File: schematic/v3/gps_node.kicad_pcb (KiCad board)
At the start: 2 copper layers, 48 x 75 mm, 69 parts, among them IC1 MCP73831/2, J1 Mounting Hole, J11 AVR ICSP, J12 UART RF, J13 LIPO_BAT, J14 SOLAR, J15 UART GPS, J16 FW_UPDATE, J17 u.FL connector, J2 Mounting Hole, J3 Mounting Hole, J4 Mounting Hole, J5 TEST Vbatt, J6 USB_OTG, J7 Test 3.3v, J8 Test Gnd, J9 Test V_bak, SW1 RS stock no. 448-0747, SW2 RESET, SW3 MODE, U1 TLV71333PDBV, U2 ublox-cam-m8q-0, U3 TLV71333PDBV, U4 ATMEGA32U4-AU, U5 RN2483, Y1 16MHz

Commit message: Started PCB layout
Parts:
- removed D2: BAS K73, Diodes_SMD:D_SOT-23_ANK
- removed J14: SOLAR, Connectors_Molex:Molex_PicoBlade_53047-0210_02x1.25mm_Straight
- added C22: 100nF, Capacitors_SMD:C_0805, F.Cu at (96.3, 65.0)
- added C23: 100nF, Capacitors_SMD:C_0805, F.Cu at (86.2, 65.0)
- added C24: 100nF, Capacitors_SMD:C_0805, F.Cu at (86.2, 66.9)
- added C25: 100nF, Capacitors_SMD:C_0805, F.Cu at (89.8, 65.0)
- C2: footprint Capacitors_SMD:C_1206 -> Capacitors_SMD:C_0805
- C3, C5, C6: value 4.7uF -> 10uF
- D3, D4: value LED_Small_ALT -> LED; footprint LEDs:LED_0805 -> LEDs:LED_0805_HandSoldering; moved to B.Cu
- D5: footprint LEDs:LED_0805 -> LEDs:LED_0805_HandSoldering
- D6: footprint LEDs:LED_0805 -> LEDs:LED_0805_HandSoldering; moved to B.Cu
- R12, R13: value 470 -> 1k
- SW2: value RESET -> SW_Push
- SW3: value MODE -> SW_Push
- moved C19 56.9 mm to (80.3, 127.8)
- moved C12 54.7 mm to (82.3, 123.2)
- moved U5 49.5 mm to (66.3, 91.2)
- moved C5 40.5 mm to (71.9, 122.9)
- moved R17 27.1 mm to (83.1, 133.1)
- moved D5 26.8 mm to (83.1, 129.0)
- moved R18 26.8 mm to (85.1, 133.1)
- moved R13 26.3 mm to (87.4, 133.0), turned to 90 degrees
- moved R12 25.9 mm to (89.7, 133.1), turned to 90 degrees
- moved D6 9.63 mm to (115.6, 125.8), turned to 0 degrees
- moved D4 5.24 mm to (115.7, 115.6), turned to 180 degrees
- moved D3 3.55 mm to (115.7, 120.7), turned to 180 degrees
- moved R10 0.19 mm to (105.2, 111.8), turned to 90 degrees
- turned R2 to 270 degrees
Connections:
- net +3V3 renamed V_3.3
- net +BATT renamed V_BATT
- net /MISO renamed /Microcontroller/MISO
- net /MOSI renamed /Microcontroller/MOSI
- net /REG_ENABLE renamed /power/REG_ENABLE
- net /SCK renamed /Microcontroller/SCK
- net /UART_AT_TO_RN renamed /Microcontroller/UART_RN_IN
- net /UART_GPS_OUT renamed /Microcontroller/UART_GPS_OUT
- net /UART_RN_TO_AT renamed /Microcontroller/UART_RN_OUT
- net /V_Charger renamed /power/V_Charger
- net /V_bak renamed V_BAK
- net /charge_status renamed /Microcontroller/CHARGE_STATUS
- net Net-(C1-Pad3) renamed /Sheet5C378858/GPS_POWER
- net Net-(J16-Pad4) renamed /Sheet5C378858/RN_PGD
- net Net-(J16-Pad5) renamed /Sheet5C378858/RN_PGC
- C12 pad 1: /V_RN -> /Sheet5C378858/RN_POWER
- C14 pad 1: Net-(C14-Pad1) -> GND
- C14 pad 2: GND -> Net-(C14-Pad2)
- C15 pad 1: Net-(C15-Pad1) -> GND
- C15 pad 2: GND -> Net-(C15-Pad2)
- C16 pad 1: Net-(C16-Pad1) -> GND
- C16 pad 2: GND -> Net-(C16-Pad2)
- C17 pad 1: Net-(C17-Pad1) -> GND
- C17 pad 2: GND -> Net-(C17-Pad2)
- C19 pad 3: /V_RN -> /Sheet5C378858/RN_POWER
- C20 pad 1: /BAT_MEASURE -> GND
- C20 pad 2: GND -> /Microcontroller/BAT_MEASURE
- C5 pad 1: /V_RN -> /Sheet5C378858/RN_POWER
- D1 pad 2: /V_Solar -> V_BUS
- F1 pad 1: VBUS -> V_BUS
- J11 pad 5: /RESET -> /Microcontroller/RESET
- J15 pad 2: /UART_GPS_IN -> /Microcontroller/UART_GPS_IN
- J16 pad 1: /RN_RESET -> /Microcontroller/RN_RESET
- J16 pad 2: /V_RN -> /Sheet5C378858/RN_POWER
- R10 pad 1: /RN_RESET -> /Sheet5C378858/RN_POWER
- R10 pad 2: /V_RN -> /Microcontroller/RN_RESET
- R11 pad 2: /BUTTON_1 -> /Microcontroller/BUTTON_1
- R12 pad 1: Net-(D3-Pad2) -> /Microcontroller/LED0
- R12 pad 2: /LED_OUT_RED -> Net-(D3-Pad2)
- R13 pad 1: Net-(D4-Pad2) -> /Microcontroller/LED1
- R13 pad 2: /LED_OUT_GRN -> Net-(D4-Pad2)
- R15 pad 2: /BAT_MEASURE -> /Microcontroller/BAT_MEASURE
- R16 pad 1: /BAT_MEASURE -> /Microcontroller/BAT_MEASURE
- R2 pad 1: /UART_GPS_IN -> Net-(R2-Pad1)
- R2 pad 2: Net-(R2-Pad2) -> /Microcontroller/UART_GPS_IN
- R4 pad 1: /USBD+ -> Net-(J6-Pad3)
- R4 pad 2: Net-(J6-Pad3) -> /Microcontroller/USBD+
- R5 pad 1: /USBD- -> Net-(J6-Pad2)
- R5 pad 2: Net-(J6-Pad2) -> /Microcontroller/USBD-
- R6 pad 2: /RESET -> /Microcontroller/RESET
- SW2 pad 1: GND -> /Microcontroller/RESET
- SW2 pad 2: /RESET -> GND
- SW3 pad 1: GND -> /Microcontroller/BUTTON_1
- SW3 pad 2: /BUTTON_1 -> GND
- U2 pad 26: Net-(R2-Pad2) -> Net-(R2-Pad1)
- U4 pad 13: /RESET -> /Microcontroller/RESET
- U4 pad 16: Net-(C15-Pad1) -> Net-(C15-Pad2)
- U4 pad 17: Net-(C14-Pad1) -> Net-(C14-Pad2)
- U4 pad 18: /BUTTON_1 -> /Microcontroller/BUTTON_1
- U4 pad 2: VBUS -> V_BUS
- U4 pad 3: /USBD- -> /Microcontroller/USBD-
- U4 pad 30: /UART_GPS_IN -> /Microcontroller/UART_GPS_IN
- U4 pad 31: /RN_RESET -> /Microcontroller/RN_RESET
- U4 pad 36: /LED_OUT_GRN -> /Microcontroller/LED1
- U4 pad 37: /LED_OUT_RED -> /Microcontroller/LED0
- U4 pad 4: /USBD+ -> /Microcontroller/USBD+
- U4 pad 41: /BAT_MEASURE -> /Microcontroller/BAT_MEASURE
- U4 pad 42: Net-(C17-Pad1) -> Net-(C17-Pad2)
- U4 pad 6: Net-(C16-Pad1) -> Net-(C16-Pad2)
- U4 pad 7: VBUS -> V_BUS
- U5 pad 12: /V_RN -> /Sheet5C378858/RN_POWER
- U5 pad 32: /RN_RESET -> /Microcontroller/RN_RESET
- U5 pad 34: /V_RN -> /Sheet5C378858/RN_POWER
- Y1 pad 1: Net-(C14-Pad1) -> Net-(C14-Pad2)
- Y1 pad 2: Net-(C15-Pad1) -> Net-(C15-Pad2)
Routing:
- net /RN_RESET: track 88.3 -> 0.00 mm, vias 5 -> 0
- net V_BUS: track 0.00 -> 79.5 mm, vias 0 -> 5
- net /LED_OUT_GRN: track 54.9 -> 0.00 mm, vias 2 -> 0
- net /LED_OUT_RED: track 52.8 -> 0.00 mm, vias 2 -> 0
- net VBUS: track 51.4 -> 0.00 mm, vias 3 -> 0
- net /UART_GPS_IN: track 46.2 -> 0.00 mm
- net /Microcontroller/UART_GPS_IN: track 0.00 -> 46.2 mm
- net /V_RN: track 43.3 -> 0.00 mm
- net GND: track 432.7 -> 395.5 mm, vias 190 -> 175
- net /V_Solar: track 28.1 -> 0.00 mm, vias 2 -> 0
- net /Microcontroller/UART_RN_OUT: track 24.8 -> 0.00 mm, vias 1 -> 0
- net /RESET: track 54.5 -> 30.5 mm, vias 4 -> 2
- net Net-(D3-Pad2): track 1.51 -> 24.8 mm, vias 0 -> 2
- net /Microcontroller/LED1: track 0.00 -> 22.6 mm, vias 0 -> 1
- net /Microcontroller/RESET: track 0.00 -> 22.1 mm, vias 0 -> 2
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
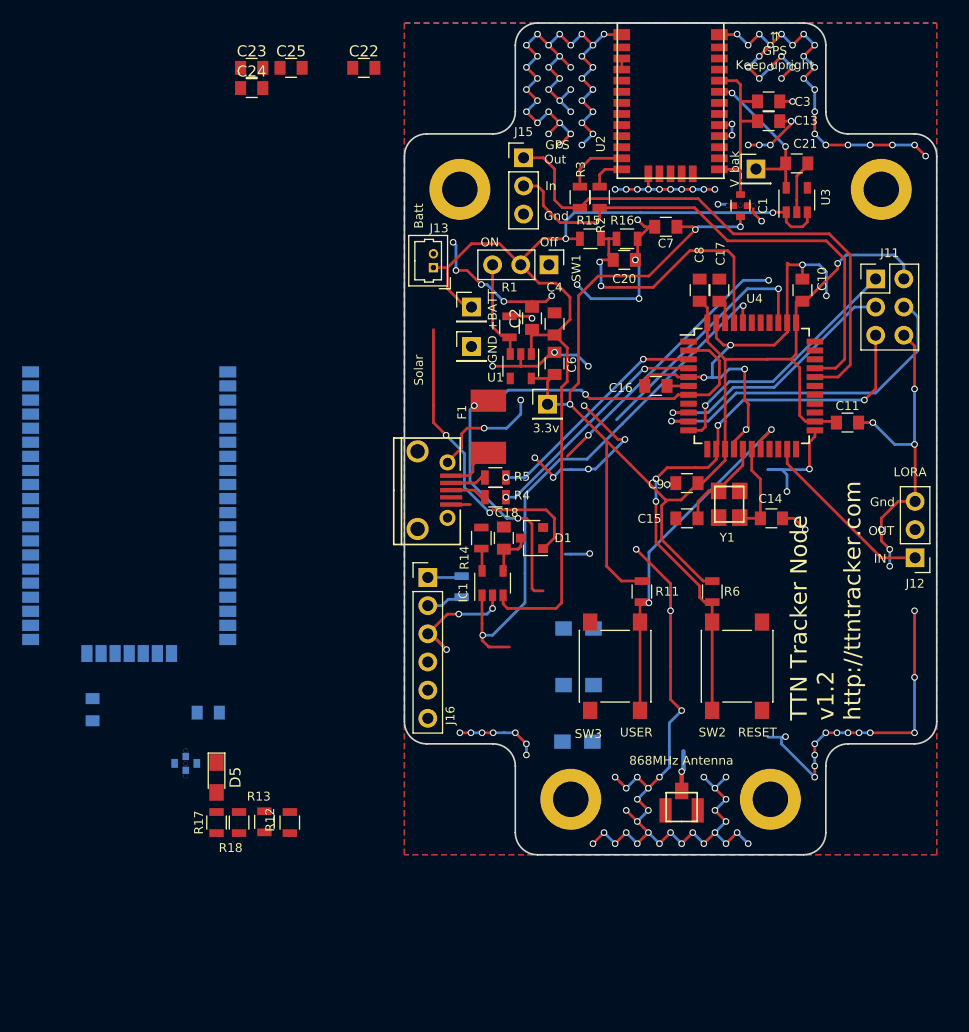
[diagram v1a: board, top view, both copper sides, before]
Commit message: Started layout work
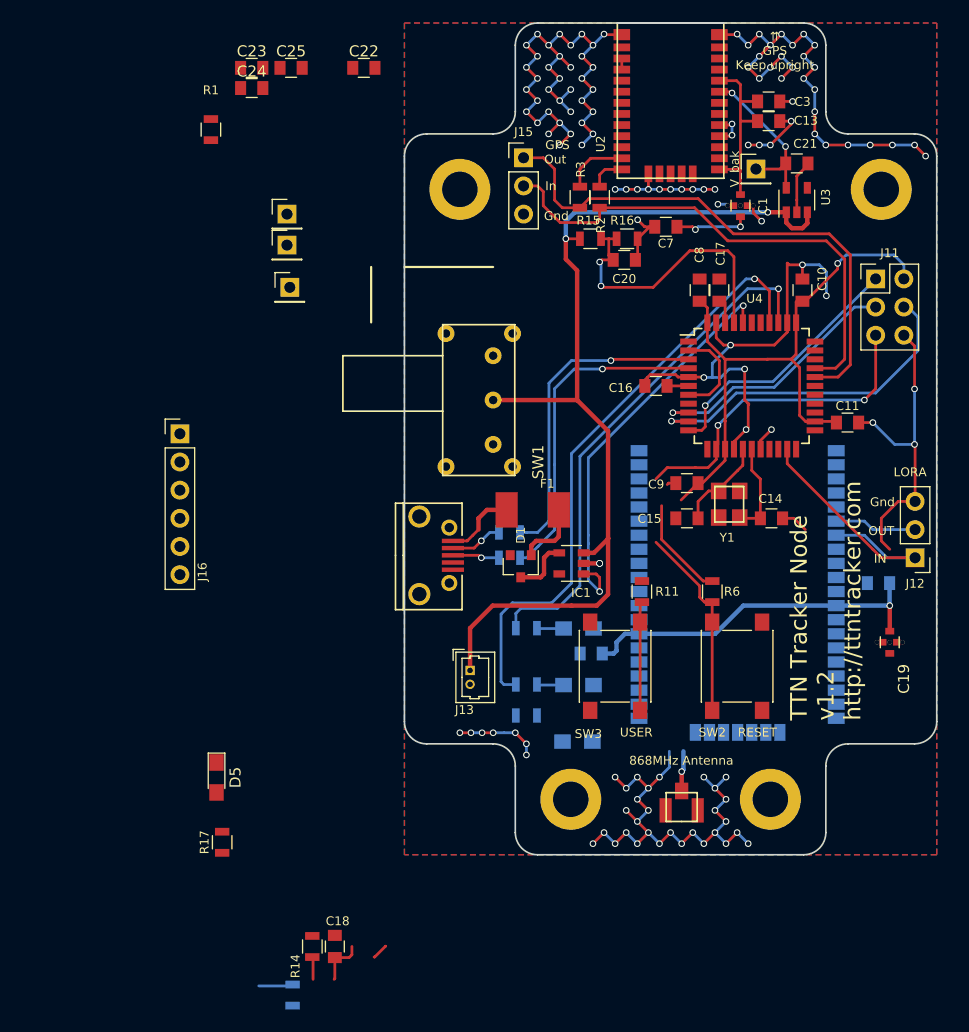
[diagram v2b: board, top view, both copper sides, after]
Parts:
- removed C2, C6: 10uF, Capacitors_SMD:C_0805
- removed C4: 100nF, Capacitors_SMD:C_0805
- removed U1: TLV71333PDBV, TO_SOT_Packages_SMD:SOT-23-5
- C19: moved to F.Cu
- R12, R13, R18, R4, R5: moved to B.Cu
- SW1: footprint Pin_Headers:Pin_Header_Straight_1x03_Pitch2.54mm -> EG1224:EG1224_Switch
- moved C5 71.8 mm to (142.7, 111.5), turned to 180 degrees
- moved C19 64.4 mm to (143.8, 116.8), turned to 90 degrees
- moved U5 55.3 mm to (121.2, 98.3)
- moved R10 39.9 mm to (89.9, 148.7)
- moved C18 39.9 mm to (93.7, 144.3)
- moved R14 39.9 mm to (91.7, 144.3)
- moved J13 36.5 mm to (105.9, 119.4), turned to 270 degrees
- moved C12 34.9 mm to (116.8, 117.9), turned to 180 degrees
- moved R1 32.3 mm to (82.5, 70.6)
- moved R13 29.4 mm to (111.0, 115.6), turned to 0 degrees
- moved R18 27.6 mm to (111.0, 123.4), turned to 0 degrees
- moved J7 27.5 mm to (89.4, 81.0)
- moved J16 25.8 mm to (79.8, 98.0)
- moved R12 24.7 mm to (111.0, 120.7), turned to 0 degrees
- moved J5 18.6 mm to (89.4, 78.2)
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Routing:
- net GND: track 395.5 -> 256.0 mm, vias 175 -> 132
- net V_BUS: track 79.5 -> 16.0 mm, vias 5 -> 0
- net V_3.3: track 129.7 -> 70.1 mm, vias 4 -> 3
- net /Microcontroller/LED0: track 0.00 -> 54.4 mm, vias 0 -> 1
- net /Microcontroller/USBD+: track 0.00 -> 29.7 mm, vias 0 -> 1
- net /Microcontroller/USBD-: track 0.00 -> 28.8 mm, vias 0 -> 1
- net /Sheet5C378858/RN_POWER: track 4.30 -> 32.5 mm, vias 0 -> 1
- net /Microcontroller/LED1: track 22.6 -> 47.1 mm
- net Net-(D3-Pad2): track 24.8 -> 2.42 mm, vias 2 -> 0
- net /USBD+: track 21.3 -> 0.00 mm, vias 2 -> 0
- net /USBD-: track 20.9 -> 0.00 mm, vias 2 -> 0
- net /BUTTON_1: track 30.9 -> 10.0 mm, vias 1 -> 0
- net /Microcontroller/CHARGE_STATUS: track 50.3 -> 36.5 mm
- net /RESET: track 30.5 -> 17.7 mm, vias 2 -> 0
- net /power/REG_ENABLE: track 9.04 -> 0.00 mm
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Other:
- board text removed: "+BATT"
- board text removed: "3.3v"
- board text removed: "Batt"
- board text removed: "GND"
- board text removed: "ON"
- board text removed: "Off"
- board text removed: "Solar"

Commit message: More layout work
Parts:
- removed D5, D6: LED, LEDs:LED_0805_HandSoldering
- added C2: 10uF, Capacitors_SMD:C_0805, F.Cu at (114.6, 95.8)
- added C4: 100nF, Capacitors_SMD:C_0805, F.Cu at (114.6, 98.6)
- added C6: 10uF, Capacitors_SMD:C_0805, F.Cu at (114.6, 88.4)
- added D2: LED_Dual_CCAA, dual_led:LED_DUAL_1206, B.Cu at (115.7, 125.8)
- added U1: TLV71333PDBV, TO_SOT_Packages_SMD:SOT-23-5, F.Cu at (114.6, 91.9)
- C19, C22, C23, C24: moved to B.Cu
- moved C24 70.9 mm to (141.5, 111.3), turned to 90 degrees
- moved R10 67.9 mm to (143.5, 106.9), turned to 270 degrees
- moved J16 67.2 mm to (146.1, 109.2)
- moved C23 57.5 mm to (117.1, 113.5), turned to 180 degrees
- moved R1 44.0 mm to (114.6, 100.8), turned to 0 degrees
- moved R14 43.2 mm to (89.8, 101.1)
- moved C22 41.2 mm to (135.4, 78.2)
- moved C18 33.9 mm to (108.0, 113.5), turned to 270 degrees
- moved R17 32.2 mm to (113.3, 122.4), turned to 270 degrees
- moved C25 26.7 mm to (78.4, 89.2)
- moved J12 5.08 mm to (146.1, 104.1)
- moved R11 1.97 mm to (121.4, 110.3)
- moved C19 1.70 mm to (142.2, 116.1)
- moved C5 0.80 mm to (143.5, 111.3), turned to 90 degrees
- moved F1 0.51 mm to (111.6, 105.4)
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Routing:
- net V_3.3: track 70.1 -> 122.4 mm, vias 3 -> 6
- net /Microcontroller/BUTTON_1: track 2.30 -> 46.5 mm, vias 1 -> 2
- net /Microcontroller/RN_RESET: track 3.10 -> 35.3 mm, vias 0 -> 1
- net /Microcontroller/RESET: track 29.2 -> 57.2 mm
- net /Sheet5C378858/RN_PGD: track 0.00 -> 26.2 mm, vias 0 -> 1
- net /Sheet5C378858/RN_PGC: track 0.00 -> 25.6 mm, vias 0 -> 1
- net V_BATT: track 88.8 -> 114.3 mm
- net /Microcontroller/CHARGE_STATUS: track 36.5 -> 58.1 mm, vias 2 -> 4
- net /power/REG_ENABLE: track 0.00 -> 19.4 mm, vias 0 -> 2
- net /RESET: track 17.7 -> 0.00 mm
- net /power/V_Charger: track 9.62 -> 22.6 mm, vias 0 -> 2
- net /Microcontroller/UART_RN_OUT: track 7.43 -> 20.0 mm, vias 0 -> 1
- net Net-(D2-Pad3): track 0.00 -> 10.6 mm, vias 0 -> 1
- net GND: track 256.0 -> 266.0 mm
- net /BUTTON_1: track 10.0 -> 0.00 mm
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
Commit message: More layout
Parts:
- moved C25 57.2 mm to (132.8, 71.6)
- moved J5 41.0 mm to (105.7, 115.8)
- moved J8 33.0 mm to (122.4, 88.4)
- moved R14 25.7 mm to (112.5, 113.0), turned to 180 degrees
- moved J7 23.2 mm to (112.3, 84.8)
- moved R17 1.80 mm to (114.8, 121.4)
- moved C21 1.63 mm to (136.7, 74.7)
- moved U3 1.63 mm to (136.7, 78.0)
- moved J13 1.52 mm to (105.9, 120.9)
- moved R11 1.08 mm to (120.9, 111.3)
- moved J9 1.02 mm to (132.6, 74.7)
- turned C17 to 270 degrees
- turned C20 to 180 degrees
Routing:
- net /Microcontroller/BAT_MEASURE: track 0.00 -> 26.6 mm, vias 0 -> 2
- net /BAT_MEASURE: track 26.6 -> 0.00 mm, vias 2 -> 0
- net V_3.3: track 122.4 -> 102.8 mm
- net GND: track 266.0 -> 276.4 mm, vias 132 -> 135
- net V_BATT: track 114.3 -> 122.7 mm
- net /Microcontroller/RN_RESET: track 35.3 -> 32.2 mm
- net Net-(IC1-Pad5): track 0.00 -> 2.55 mm
- net Net-(C17-Pad2): track 0.00 -> 1.82 mm
- net Net-(C17-Pad1): track 1.82 -> 0.00 mm
- net /Sheet5C378858/GPS_POWER: track 17.0 -> 18.5 mm
- net V_BAK: track 14.7 -> 15.9 mm, vias 2 -> 1
- net /Microcontroller/BUTTON_1: track 46.5 -> 45.4 mm
- net Net-(D2-Pad3): track 10.6 -> 9.73 mm

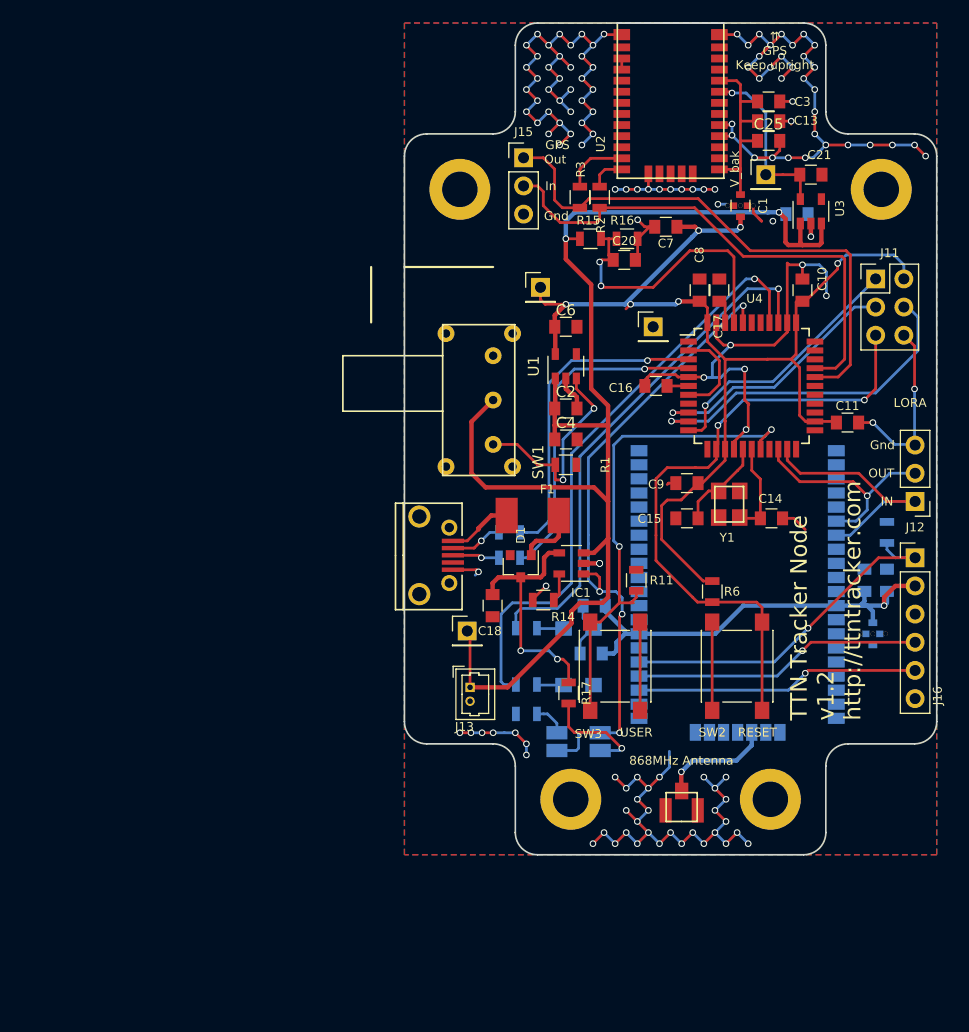
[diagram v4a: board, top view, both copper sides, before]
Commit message: Adds Accelerometer, layout almost done
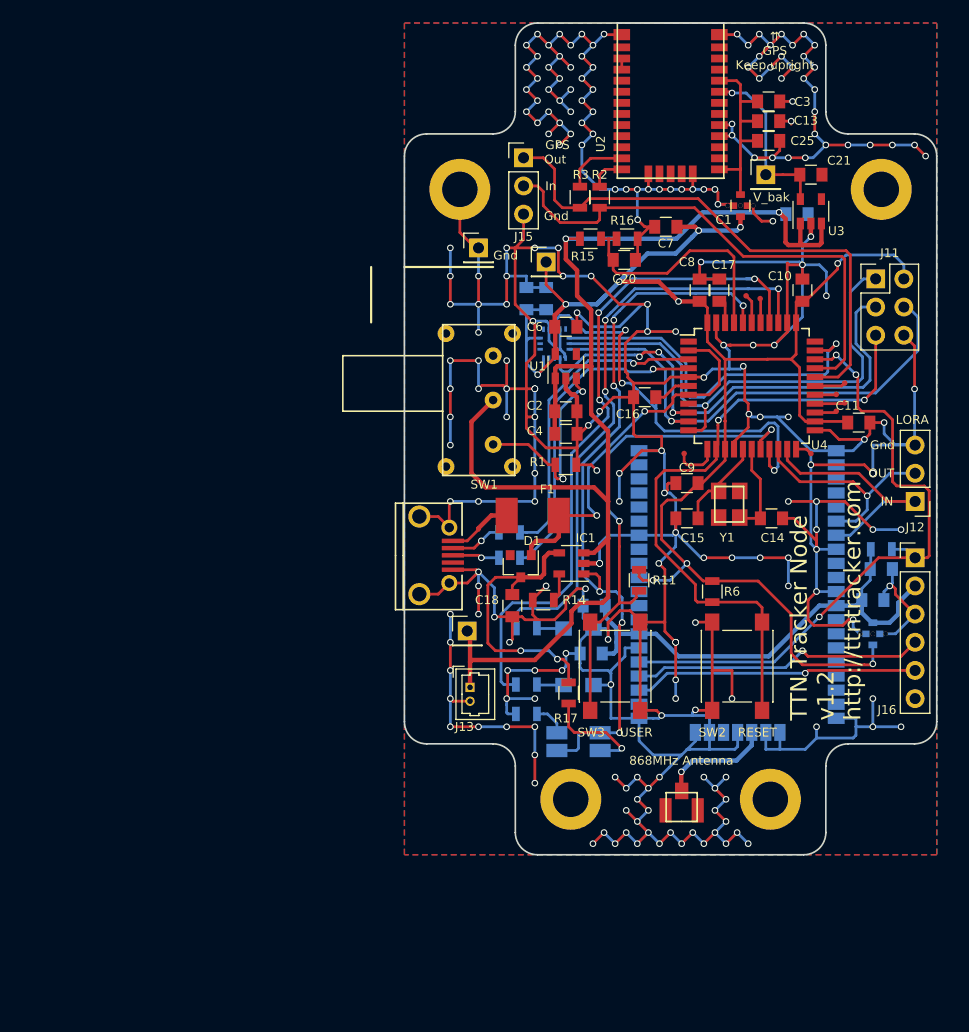
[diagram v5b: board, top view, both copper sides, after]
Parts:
- added C26: 10uF, Capacitors_SMD:C_0805, B.Cu at (112.8, 85.9)
- added C27: 100nF, Capacitors_SMD:C_0805, B.Cu at (111.0, 85.9)
- added TP1: TestPoint, test_pad:test_pad, F.Cu at (139.7, 93.5)
- added TP2: TestPoint, test_pad:test_pad, F.Cu at (125.2, 99.8)
- added TP3: TestPoint, test_pad:test_pad, F.Cu at (138.9, 96.0)
- added TP4: TestPoint, test_pad:test_pad, F.Cu at (136.7, 99.8)
- added TP5: TestPoint, test_pad:test_pad, F.Cu at (139.7, 95.2)
- added TP6: TestPoint, test_pad:test_pad, F.Cu at (138.9, 94.5)
- added TP7: TestPoint, test_pad:test_pad, F.Cu at (130.8, 85.6)
- added TP8: TestPoint, test_pad:test_pad, F.Cu at (132.1, 85.9)
- added U6: LIS3DH, lga_16:LGA16-pitch0.5-3mmx3mm, B.Cu at (113.5, 89.9)
- moved J8 17.3 mm to (106.7, 81.3)
- moved J7 2.34 mm to (112.8, 82.5)
- moved C5 2.18 mm to (142.2, 113.0), turned to 0 degrees
- moved C24 1.83 mm to (143.0, 110.2), turned to 0 degrees
- moved C18 1.78 mm to (109.7, 113.5)
- moved R10 1.61 mm to (143.0, 108.5), turned to 0 degrees
- moved C16 1.44 mm to (121.7, 94.7), turned to 0 degrees
- moved C11 1.02 mm to (141.0, 97.0)
- moved C4 0.51 mm to (114.6, 98.0)
- moved C2 0.25 mm to (114.6, 96.0)
- moved R11 0.25 mm to (121.2, 111.3)
- turned C14 to 180 degrees
- turned C15 to 0 degrees
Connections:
- net /Microcontroller/MISO renamed /Microcontroller/SPI_MISO
- net /Microcontroller/MOSI renamed /Microcontroller/SPI_MOSI
- net /Microcontroller/SCK renamed /Microcontroller/SPI_CLK
- U4 pad 12: (no net) -> Net-(TP2-Pad1)
- U4 pad 19: (no net) -> /Microcontroller/ACCEL_INT
- U4 pad 22: (no net) -> Net-(TP4-Pad1)
- U4 pad 25: (no net) -> Net-(TP3-Pad1)
- U4 pad 26: (no net) -> Net-(TP5-Pad1)
- U4 pad 27: (no net) -> Net-(TP6-Pad1)
- U4 pad 28: (no net) -> Net-(TP1-Pad1)
- U4 pad 32: (no net) -> /Microcontroller/ACCEL_CS
- U4 pad 38: (no net) -> Net-(TP8-Pad1)
- U4 pad 39: (no net) -> Net-(TP7-Pad1)
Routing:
- net GND: track 276.4 -> 778.6 mm, vias 135 -> 230
- net V_3.3: track 102.8 -> 147.5 mm, vias 6 -> 10
- net /Microcontroller/ACCEL_INT: track 0.00 -> 37.0 mm, vias 0 -> 3
- net /Microcontroller/ACCEL_CS: track 0.00 -> 33.1 mm, vias 0 -> 1
- net /Microcontroller/RN_RESET: track 32.2 -> 58.9 mm, vias 1 -> 3
- net /Microcontroller/SPI_MISO: track 23.9 -> 46.3 mm
- net /Microcontroller/SPI_CLK: track 23.7 -> 45.9 mm, vias 1 -> 3
- net V_BUS: track 14.1 -> 34.1 mm, vias 0 -> 2
- net /Microcontroller/SPI_MOSI: track 31.2 -> 45.5 mm
- net Net-(C15-Pad1): track 8.49 -> 0.00 mm
- net Net-(C14-Pad1): track 8.45 -> 0.00 mm
- net Net-(C15-Pad2): track 0.00 -> 8.44 mm
- net /Microcontroller/CHARGE_STATUS: track 58.1 -> 66.3 mm, vias 4 -> 6
- net /Microcontroller/LED0: track 54.4 -> 61.9 mm, vias 1 -> 3
- net /Microcontroller/LED1: track 47.1 -> 53.8 mm, vias 1 -> 3
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
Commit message: Fixed battery connector, started bom
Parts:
- J13: footprint Connectors_Molex:Molex_PicoBlade_53047-0210_02x1.25mm_Straight -> Connectors_Molex:Molex_MicroLatch-53253-0270_02x2.00mm_Straight
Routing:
- net GND: track 778.6 -> 776.7 mm
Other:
- board text added: "+"
- board text added: "-"
